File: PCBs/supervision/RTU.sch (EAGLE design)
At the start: 17 parts, among them IC1 LM1117T-1.8, IC2 7805T, M1 WIRELESS-NRF24L01, U1 ESP-WROOM-32, U2 MICROSD_CATALEX, U3 DS1307Z, Y2 32kHz

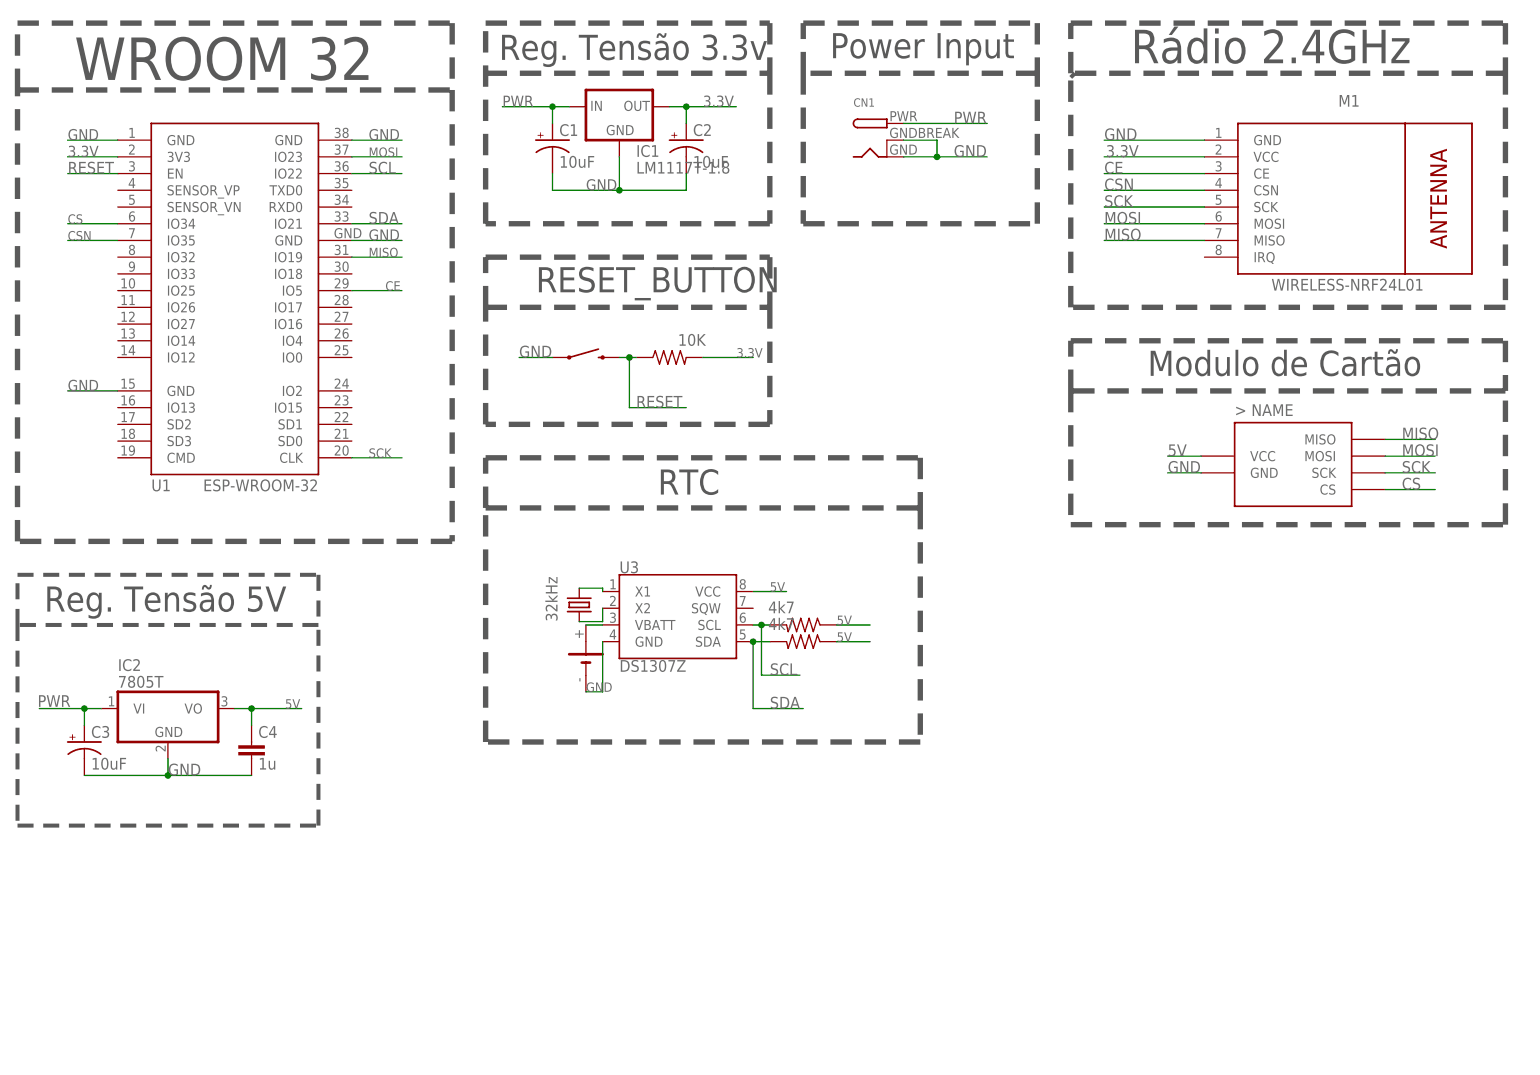
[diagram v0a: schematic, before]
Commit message: Alterações na PCB do sistema supervisorio
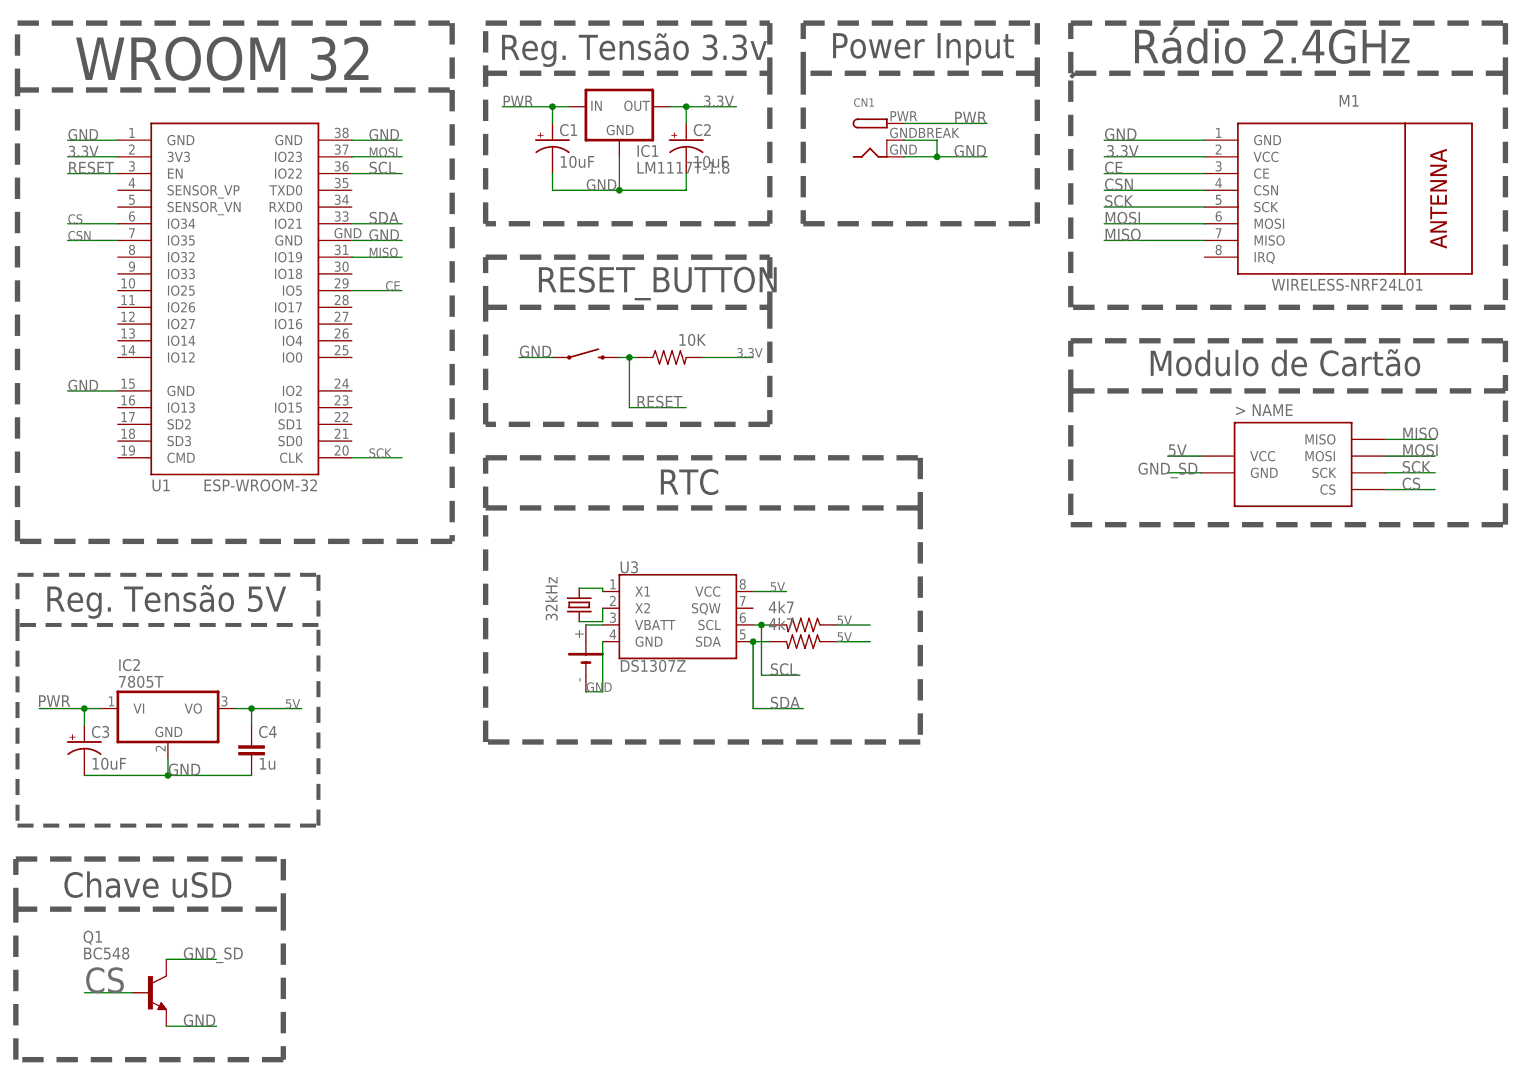
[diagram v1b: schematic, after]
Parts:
- added Q1: BC548, transistor-npn:BC548
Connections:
- new net GND_SD: Q1.C, U2.GND
- net CS: now also Q1.B
- net GND: now also Q1.E; no longer U2.GND
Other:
- note added: "Chave uSD"
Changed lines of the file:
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@@
 <part name="C3" library="SparkFun-Capacitors" deviceset="10UF-POLAR" device="-RADIAL-2.5MM-25V-20%" value="10uF"/>
 <part name="C4" library="resistor" deviceset="C-EU" device="025-024X044" value="1u"/>
+<part name="Q1" library="transistor-npn" library_urn="urn:adsk.eagle:library:398" deviceset="BC548*" device="" package3d_urn="urn:adsk.eagle:package:28989/2"/>
 </parts>
 <sheets>
@@
 <wire x1="55.88" y1="83.82" x2="55.88" y2="76.2" width="0.6096" layer="97" style="shortdash"/>
 <text x="14.224" y="78.232" size="3.81" layer="97">Reg. Tensão 5V</text>
+<wire x1="9.906" y1="10.16" x2="9.906" y2="33.02" width="0.8128" layer="97" style="shortdash"/>
+<wire x1="9.906" y1="33.02" x2="50.546" y2="33.02" width="0.8128" layer="97" style="shortdash"/>
+<wire x1="50.546" y1="33.02" x2="50.546" y2="10.16" width="0.8128" layer="97" style="shortdash"/>
+<wire x1="50.546" y1="10.16" x2="9.906" y2="10.16" width="0.8128" layer="97" style="shortdash"/>
+<wire x1="9.906" y1="33.02" x2="9.906" y2="40.64" width="0.8128" layer="97" style="shortdash"/>
+<wire x1="9.906" y1="40.64" x2="50.546" y2="40.64" width="0.8128" layer="97" style="shortdash"/>
+<wire x1="50.546" y1="40.64" x2="50.546" y2="33.02" width="0.8128" layer="97" style="shortdash"/>
+<text x="17.018" y="34.798" size="3.81" layer="97">Chave uSD</text>
 </plain>
 <instances>
@@
 <attribute name="NAME" x="46.736" y="59.055" size="1.778" layer="95"/>
 <attribute name="VALUE" x="46.736" y="54.229" size="1.778" layer="96"/>
+</instance>
+<instance part="Q1" gate="G$1" x="30.226" y="20.32" smashed="yes">
+<attribute name="NAME" x="20.066" y="27.94" size="1.778" layer="95"/>
+<attribute name="VALUE" x="20.066" y="25.4" size="1.778" layer="96"/>
 </instance>
 </instances>
@@
 </segment>
 <segment>
-<pinref part="U2" gate="G$1" pin="GND"/>
-<wire x1="189.992" y1="99.314" x2="184.912" y2="99.314" width="0.1524" layer="91"/>
-<label x="184.912" y="99.314" size="1.778" layer="95"/>
-</segment>
-<segment>
 <pinref part="C3" gate="G$1" pin="-"/>
 <pinref part="C4" gate="G$1" pin="2"/>
@@
 <label x="96.52" y="66.04" size="1.4224" layer="95"/>
 </segment>
+<segment>
+<pinref part="Q1" gate="G$1" pin="E"/>
+<wire x1="32.766" y1="15.24" x2="40.386" y2="15.24" width="0.1524" layer="91"/>
+<label x="35.306" y="15.24" size="1.778" layer="95"/>
+</segment>
 </net>
 <net name="3.3V" class="0">
@@
 <label x="17.78" y="137.16" size="1.4224" layer="95"/>
 </segment>
+<segment>
+<pinref part="Q1" gate="G$1" pin="B"/>
+<wire x1="27.686" y1="20.32" x2="20.32" y2="20.32" width="0.1524" layer="91"/>
+<label x="20.32" y="20.32" size="3.81" layer="95"/>
+</segment>
 </net>
 <net name="N$1" class="0">
@@
 </segment>
 </net>
+<net name="GND_SD" class="0">
+<segment>
+<pinref part="Q1" gate="G$1" pin="C"/>
+<wire x1="32.766" y1="25.4" x2="40.386" y2="25.4" width="0.1524" layer="91"/>
+<label x="35.306" y="25.4" size="1.778" layer="95"/>
+</segment>
+<segment>
+<pinref part="U2" gate="G$1" pin="GND"/>
+<wire x1="189.992" y1="99.314" x2="184.912" y2="99.314" width="0.1524" layer="91"/>
+<label x="180.34" y="99.06" size="1.778" layer="95"/>
+</segment>
+</net>

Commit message: Re-prototipação da PCB do sistema supervisorio
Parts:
- removed C1, C2: 10uF, SparkFun-Capacitors:10UF-POLAR-RADIAL-2.5MM-25V-20%
- removed IC1: LM1117T-1.8, lm1117:LM1117T-1.8
- removed M1: WIRELESS-NRF24L01, diy-modules:WIRELESS-NRF24L01
- removed R1: 10K, adafruit:R-US_0204/7
- removed RESET_BUTTON: MOMENTARY-SWITCH-SPST-PTH-6.0MM, SparkFun-Switches:MOMENTARY-SWITCH-SPST-PTH-6.0MM
- removed U1: ESP-WROOM-32, esp32:ESP-WROOM-32
- added U$1: ESP32_DEVKIT, DOIT_ESP32_DEVKIT:ESP32_DEVKIT
- added U$2: NRF24L01, Clean-Kong:NRF24L01
- IC2: value 7805T -> 7805DT; device linear:7805T -> linear:7805DT
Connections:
- removed net 3.3V: C2.+, IC1.OUT, M1.VCC, R1.2, U1.3V3
- removed net RESET: R1.1, RESET_BUTTON.2, U1.EN
- new net 3V3: U$1.3V3, U$2.VCC
- new net USD: Q1.B, U$1.D34
- net CE: now also U$1.D4, U$2.CE; no longer M1.CE, U1.IO5
- net CS: no longer Q1.B, U1.IO34
- net CSN: now also U$1.D5, U$2.CSN; no longer M1.CSN, U1.IO35
- net GND: now also U$1.GND@1, U$1.GND@2, U$2.GND; no longer C1.-, C2.-, IC1.GND, M1.GND, RESET_BUTTON.1, U1.GND@1, U1.GND@2, U1.GND@3, U1.GND@4
- net MISO: now also U$1.D19, U$2.MISO; no longer M1.MISO, U1.IO19
- net MOSI: now also U$1.D23, U$2.MOSI; no longer M1.MOSI, U1.IO23
- net PWR: now also U$1.VIN; no longer C1.+, IC1.IN
- net SCK: now also U$1.D18, U$2.SCK; no longer M1.SCK, U1.CLK
- net SCL: now also U$1.D22; no longer U1.IO22
- net SDA: now also U$1.D21; no longer U1.IO21
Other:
- note added: "Node MCU - 32"
- note removed: "Reg. Tensão 3.3v"
- note removed: "WROOM 32"
- moved on the sheet: CN1, U3
